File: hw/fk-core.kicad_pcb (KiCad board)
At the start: 2 copper layers, 98.8 x 37 mm, 110 parts, among them J1 RF-SMA-EDGE, J10 S2B-PH-SM4-TB, J11 RF-SMA-EDGE, J4 Conn_01x01, J5 Conn_01x03, J6 Conn_01x05, J7 CONN-HDR-2x5, J9 MICRO-USB, M1 MOUNT_HOLE, M3 MOUNT_HOLE, M4 MOUNT_HOLE, M6 MOUNT_HOLE, M7 MICROSD, Q1 2N7002LT1G, Q2 2N7002LT1G, Q3 2N7002LT1G, Q4 2N7002LT1G, SW1 SPNO, SW2 SPNO, U1 ATWINC1500-MR210PA, U10 FGPMMOPA6H, U11 MAX1704XX, U2 ATSAMD21G18A-AU, U3 RFM95W, U4 24AA02E64, U5 S25FL116K0XMFI041, U6 BQ24074RGTT, U7 PCF8523, U8 MCP1700T-3302E/MB, U9 ISL8541x, Y1 FC-135, Y2 FC-135

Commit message: Fix USB footprint with the oval drills.
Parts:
- J9: footprint RocketScreamKicadLibrary:MICRO-USB -> conservify:MICRO-USB
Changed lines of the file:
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@@
       (net 2 3V3) (solder_mask_margin 0.1))
   )
-  (module RocketScreamKicadLibrary:MICRO-USB (layer F.Cu)
-    (at 80.9752 122.8344 270)
-    (tags MICRO-USB)
-    (fp_text reference J9 (at 0 -3.556 270) (layer F.SilkS) hide
-      (effects (font (size 1 1) (thickness 0.15)))
-    )
-    (fp_text value MICRO-USB (at 0 4.318 270) (layer F.Fab) hide
-      (effects (font (size 1 1) (thickness 0.15)))
-    )
-    (fp_line (start -4.55 -2.4) (end -4.55 3.45) (layer F.CrtYd) (width 0.05))
-    (fp_line (start -4.55 3.45) (end 4.55 3.45) (layer F.CrtYd) (width 0.05))
-    (fp_line (start 4.55 3.45) (end 4.55 -2.4) (layer F.CrtYd) (width 0.05))
-    (fp_line (start 4.55 -2.4) (end -4.55 -2.4) (layer F.CrtYd) (width 0.05))
-    (fp_circle (center -1.746 -2.608) (end -1.796 -2.658) (layer F.SilkS) (width 0.3))
-    (fp_line (start 3.8 0) (end 3.8 -1.55) (layer F.SilkS) (width 0.15))
-    (fp_line (start 3.8 -1.55) (end 3.25 -1.55) (layer F.SilkS) (width 0.15))
-    (fp_line (start -3.8 0) (end -3.8 -1.55) (layer F.SilkS) (width 0.15))
-    (fp_line (start -3.8 -1.55) (end -3.25 -1.55) (layer F.SilkS) (width 0.15))
-    (fp_line (start 3.8 2.2) (end 3.8 3.3) (layer F.SilkS) (width 0.15))
-    (fp_line (start -3.8 3.3) (end -3.8 2.2) (layer F.SilkS) (width 0.15))
-    (fp_line (start -3.8 3.3) (end 3.8 3.3) (layer F.SilkS) (width 0.15))
-    (pad 1 smd rect (at -1.3 -1.45 270) (size 0.4 1.35) (layers F.Cu F.Paste F.Mask)
-      (net 28 VUSB))
-    (pad 2 smd rect (at -0.65 -1.45 270) (size 0.4 1.35) (layers F.Cu F.Paste F.Mask)
-      (net 15 /USB-))
-    (pad 3 smd rect (at 0 -1.45 270) (size 0.4 1.35) (layers F.Cu F.Paste F.Mask)
-      (net 16 /USB+))
-    (pad 4 smd rect (at 0.65 -1.45 270) (size 0.4 1.35) (layers F.Cu F.Paste F.Mask)
-      (net 62 "Net-(J9-Pad4)"))
-    (pad 5 smd rect (at 1.3 -1.45 270) (size 0.4 1.35) (layers F.Cu F.Paste F.Mask)
-      (net 1 GND))
-    (pad 6 thru_hole circle (at -2.425 -1.525 270) (size 1.2 1.2) (drill 0.7) (layers *.Cu *.Mask F.SilkS)
-      (net 40 "Net-(C14-Pad1)"))
-    (pad 7 thru_hole circle (at 2.425 -1.525 270) (size 1.2 1.2) (drill 0.7) (layers *.Cu *.Mask F.SilkS)
-      (net 123 "Net-(J9-Pad7)"))
-    (pad 8 thru_hole oval (at -3.625 1.125 270) (size 1.3 1.7) (drill oval 0.7 1.1) (layers *.Cu *.Mask F.SilkS)
-      (net 63 "Net-(J9-Pad8)"))
-    (pad 9 thru_hole oval (at 3.625 1.125 270) (size 1.3 1.7) (drill oval 0.7 1.1) (layers *.Cu *.Mask F.SilkS)
-      (net 64 "Net-(J9-Pad9)"))
-  )
   (module RocketScreamKicadLibrary:S2B-PH-SM4-TB (layer F.Cu)
     (at 85.2452 141.726)
@@
       (net 131 "Net-(U3-Pad16)"))
   )
+  (module conservify:MICRO-USB (layer F.Cu)
+    (at 80.9752 122.8344 270)
+    (tags MICRO-USB)
+    (fp_text reference J9 (at -26.162 0 270) (layer F.SilkS) hide
+      (effects (font (size 0.8 0.8) (thickness 0.15)))
+    )
+    (fp_text value MICRO-USB (at 0 4.318 270) (layer F.Fab) hide
+      (effects (font (size 0.8 0.8) (thickness 0.15)))
+    )
+    (fp_line (start -4.55 -2.4) (end -4.55 3.45) (layer F.CrtYd) (width 0.05))
+    (fp_line (start -4.55 3.45) (end 4.55 3.45) (layer F.CrtYd) (width 0.05))
+    (fp_line (start 4.55 3.45) (end 4.55 -2.4) (layer F.CrtYd) (width 0.05))
+    (fp_line (start 4.55 -2.4) (end -4.55 -2.4) (layer F.CrtYd) (width 0.05))
+    (fp_circle (center -1.746 -2.608) (end -1.796 -2.658) (layer F.SilkS) (width 0.3))
+    (fp_line (start 3.8 0) (end 3.8 -1.55) (layer F.SilkS) (width 0.15))
+    (fp_line (start 3.8 -1.55) (end 3.25 -1.55) (layer F.SilkS) (width 0.15))
+    (fp_line (start -3.8 0) (end -3.8 -1.55) (layer F.SilkS) (width 0.15))
+    (fp_line (start -3.8 -1.55) (end -3.25 -1.55) (layer F.SilkS) (width 0.15))
+    (fp_line (start 3.8 2.2) (end 3.8 3.3) (layer F.SilkS) (width 0.15))
+    (fp_line (start -3.8 3.3) (end -3.8 2.2) (layer F.SilkS) (width 0.15))
+    (fp_line (start -3.8 3.3) (end 3.8 3.3) (layer F.SilkS) (width 0.15))
+    (pad 1 smd rect (at -1.3 -1.45 270) (size 0.4 1.35) (layers F.Cu F.Paste F.Mask)
+      (net 28 VUSB))
+    (pad 2 smd rect (at -0.65 -1.45 270) (size 0.4 1.35) (layers F.Cu F.Paste F.Mask)
+      (net 15 /USB-))
+    (pad 3 smd rect (at 0 -1.45 270) (size 0.4 1.35) (layers F.Cu F.Paste F.Mask)
+      (net 16 /USB+))
+    (pad 4 smd rect (at 0.65 -1.45 270) (size 0.4 1.35) (layers F.Cu F.Paste F.Mask)
+      (net 62 "Net-(J9-Pad4)"))
+    (pad 5 smd rect (at 1.3 -1.45 270) (size 0.4 1.35) (layers F.Cu F.Paste F.Mask)
+      (net 1 GND))
+    (pad 6 thru_hole circle (at -2.425 -1.525 270) (size 1.2 1.2) (drill 0.7) (layers *.Cu *.Mask F.Paste)
+      (net 40 "Net-(C14-Pad1)"))
+    (pad 7 thru_hole circle (at 2.425 -1.525 270) (size 1.2 1.2) (drill 0.7) (layers *.Cu *.Mask F.Paste)
+      (net 123 "Net-(J9-Pad7)"))
+    (pad 8 thru_hole circle (at -3.625 1.125 270) (size 1.7 1.7) (drill oval 1.1) (layers *.Cu *.Mask F.Paste)
+      (net 63 "Net-(J9-Pad8)"))
+    (pad 9 thru_hole circle (at 3.625 1.125 270) (size 1.7 1.7) (drill oval 1.1) (layers *.Cu *.Mask F.Paste)
+      (net 64 "Net-(J9-Pad9)"))
+  )
   (gr_line (start 176.164 145.3896) (end 176.164 111.2266) (layer Edge.Cuts) (width 0.15))
   (gr_text DATA (at 94.8817 141.1351 270) (layer F.SilkS)
@@
     (connect_pads (clearance 0.2032))
     (min_thickness 0.2032)
-    (fill (arc_segments 32) (thermal_gap 0.254) (thermal_bridge_width 0.254))
+    (fill yes (arc_segments 32) (thermal_gap 0.254) (thermal_bridge_width 0.254))
     (polygon
       (pts
@@
     (connect_pads (clearance 0.2032))
     (min_thickness 0.2032)
-    (fill (arc_segments 32) (thermal_gap 0.254) (thermal_bridge_width 0.254))
+    (fill yes (arc_segments 32) (thermal_gap 0.254) (thermal_bridge_width 0.254))
     (polygon
       (pts
@@
     (connect_pads (clearance 0.2032))
     (min_thickness 0.2032)
-    (fill (arc_segments 32) (thermal_gap 0.254) (thermal_bridge_width 0.254))
+    (fill yes (arc_segments 32) (thermal_gap 0.254) (thermal_bridge_width 0.254))
     (polygon
       (pts
@@
     (connect_pads (clearance 0.2032))
     (min_thickness 0.2032)
-    (fill (arc_segments 32) (thermal_gap 0.254) (thermal_bridge_width 0.254))
+    (fill yes (arc_segments 32) (thermal_gap 0.254) (thermal_bridge_width 0.254))
     (polygon
       (pts
@@
     (connect_pads (clearance 0.2032))
     (min_thickness 0.2032)
-    (fill (arc_segments 32) (thermal_gap 0.254) (thermal_bridge_width 0.254))
+    (fill yes (arc_segments 32) (thermal_gap 0.254) (thermal_bridge_width 0.254))
     (polygon
       (pts
@@
     (connect_pads (clearance 0.2032))
     (min_thickness 0.2032)
-    (fill (arc_segments 32) (thermal_gap 0.254) (thermal_bridge_width 0.254))
+    (fill yes (arc_segments 32) (thermal_gap 0.254) (thermal_bridge_width 0.254))
     (polygon
       (pts
@@
     (connect_pads (clearance 0.2032))
     (min_thickness 0.2032)
-    (fill (arc_segments 32) (thermal_gap 0.254) (thermal_bridge_width 0.254))
+    (fill yes (arc_segments 32) (thermal_gap 0.254) (thermal_bridge_width 0.254))
     (polygon
       (pts
@@
     (connect_pads (clearance 0.2032))
     (min_thickness 0.2032)
-    (fill (arc_segments 32) (thermal_gap 0.254) (thermal_bridge_width 0.254))
+    (fill yes (arc_segments 32) (thermal_gap 0.254) (thermal_bridge_width 0.254))
     (polygon
       (pts

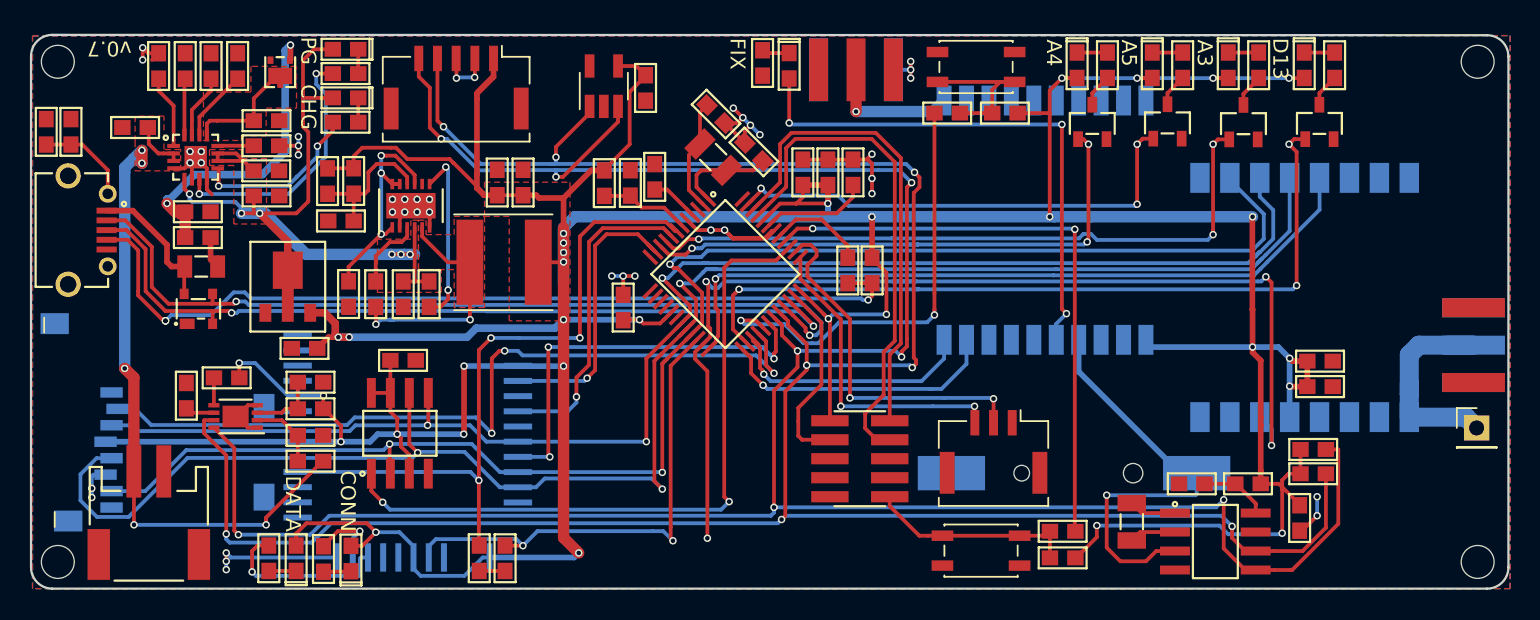
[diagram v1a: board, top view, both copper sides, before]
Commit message: Moving some parts in from the edge.
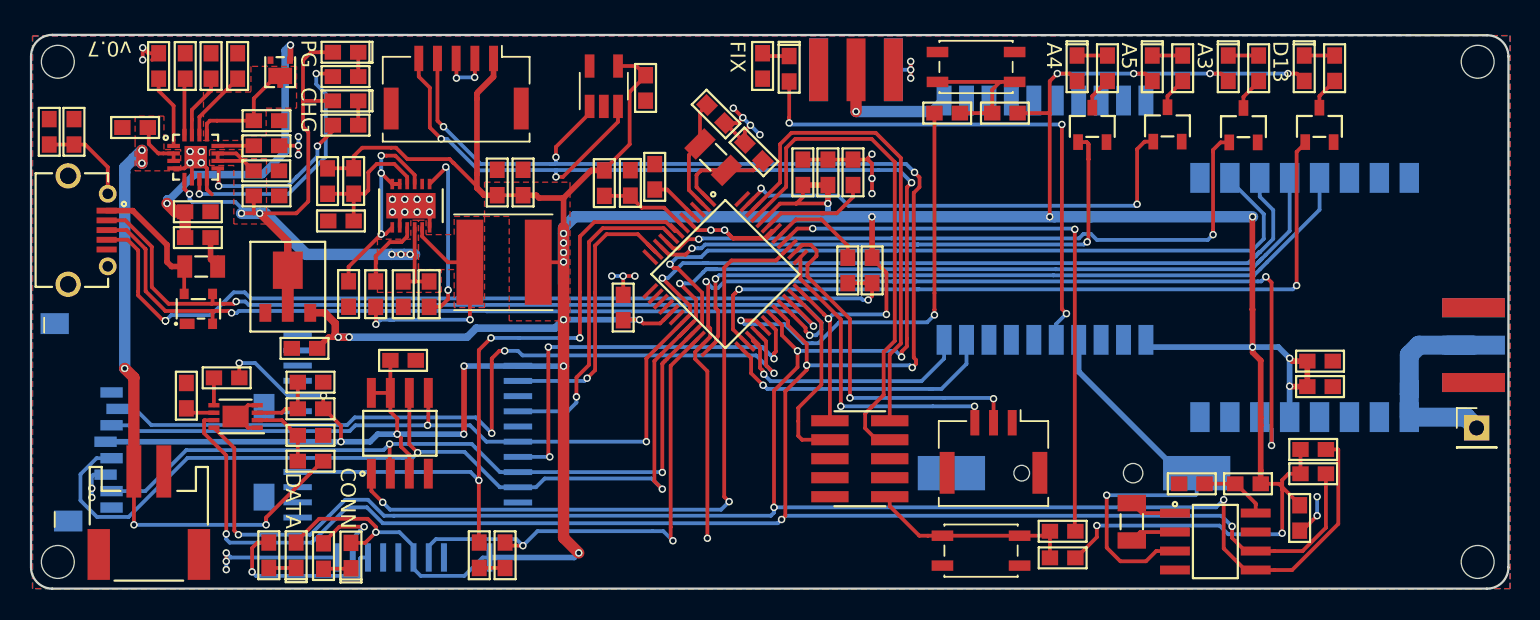
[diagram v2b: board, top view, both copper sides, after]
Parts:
- moved R5 0.20 mm to (96.9, 144.6)
- moved C14 0.20 mm to (80.2, 116.3)
- moved D1 0.20 mm to (162.5, 112.0)
- moved D10 0.20 mm to (98.4, 114.2)
- moved D11 0.20 mm to (128.1, 112.0)
- moved D4 0.20 mm to (157.4, 112.0)
- moved D5 0.20 mm to (147.3, 112.0)
- moved D6 0.20 mm to (152.3, 112.0)
- moved D9 0.20 mm to (98.4, 110.9)
- moved Q1 0.20 mm to (163.5, 115.8)
- moved Q2 0.20 mm to (158.4, 115.8)
- moved Q3 0.20 mm to (148.3, 115.8)
- moved Q4 0.20 mm to (153.4, 115.8)
- moved R18 0.20 mm to (159.5, 112.0)
- moved R19 0.20 mm to (149.4, 112.0)
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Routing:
- net 3V3: track 357.6 -> 359.5 mm
- net /D13: track 52.8 -> 51.8 mm, vias 3 -> 2
- net /A4: track 37.3 -> 38.2 mm, vias 3 -> 2
- net /SDA: track 172.4 -> 173.3 mm
- net /SCL: track 168.3 -> 169.2 mm
- net Net-(R5-Pad1): track 4.83 -> 5.58 mm
- net /A3: track 44.7 -> 44.4 mm, vias 3 -> 2
- net /A5: track 32.4 -> 32.1 mm, vias 3 -> 2
